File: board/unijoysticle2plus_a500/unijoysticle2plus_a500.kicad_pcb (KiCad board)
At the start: 4 copper layers, 62 x 49 mm, 44 parts, among them J1 DB9_Female, J2 DB9_Female, J3 USB_B_Micro, Q1 S8050, Q2 S8050, SW1 RESET, SW2 JOY SWAP, SW3 BOOT, U1 74HC05, U2 74HC05, U3 74HC05, U4 ESP32-WROOM-32E, U5 AMS1117-3.3, U6 CH340C

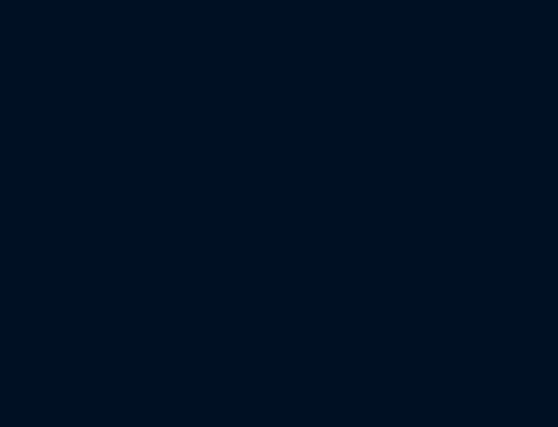
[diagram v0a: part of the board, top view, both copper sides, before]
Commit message: a500: remove duplicate symbols
It is able to run the EDR checks with 5 warnings.
Only one looks worth taking a look at.
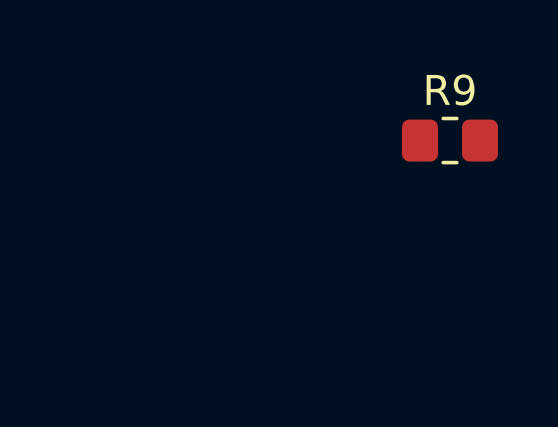
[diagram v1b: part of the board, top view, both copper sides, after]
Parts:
- added R9: 10k, Resistor_SMD:R_0805_2012Metric_Pad1.20x1.40mm_HandSolder, F.Cu at (151.9, 67.7)
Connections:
- net /ESP_BOOT renamed /ESP32/ESP_BOOT
- net /ESP_EN renamed /ESP32/ESP_EN
- net /ESP_RXD renamed UART_TX
- net /ESP_TXD renamed UART_RX
- net /GPIO34 renamed GPIO_SWITCH_USER1
- net /GPIO35 renamed GPIO_SWITCH_USER2
- net /GPIO39 renamed GPIO_39
- net /USBD+ renamed /USB Serial & Power/USBD+
- net /USBD- renamed /USB Serial & Power/USBD-
- C10 pad 2: GND -> GPIO_BOOTSTRAP_04
- C11 pad 2: GND -> GPIO_BOOTSTRAP_04
- C12 pad 1: GND -> GPIO_BOOTSTRAP_04
- C13 pad 1: GND -> GPIO_BOOTSTRAP_04
- C4 pad 2: GND -> GPIO_BOOTSTRAP_04
- C5 pad 2: GND -> GPIO_BOOTSTRAP_04
- C6 pad 1: GND -> GPIO_BOOTSTRAP_04
- C7 pad 2: GND -> GPIO_BOOTSTRAP_04
- C8 pad 2: GND -> GPIO_BOOTSTRAP_04
- C9 pad 2: GND -> GPIO_BOOTSTRAP_04
- H1 pad 1: GND -> GPIO_BOOTSTRAP_04
- H2 pad 1: GND -> GPIO_BOOTSTRAP_04
- J3 pad 5: GND -> GPIO_BOOTSTRAP_04
- Q1 pad 2: /RTS_PROG -> RTS_PROG
- Q2 pad 2: /DTR_PROG -> DTR_PROG
- R8 pad 1: Net-(Q2-Pad1) -> Net-(Q1-Pad1)
- R8 pad 2: /RTS_PROG -> DTR_PROG
- SW1 pad 1: GND -> GPIO_BOOTSTRAP_04
- SW3 pad 1: GND -> GPIO_BOOTSTRAP_04
- U4 pad 1: GND -> GPIO_BOOTSTRAP_04
- U4 pad 10: /GPIO_J2_DOWN -> GPIO_J2_DOWN
- U4 pad 11: /GPIO_J1_UP -> GPIO_J1_UP
- U4 pad 12: /GPIO_J2_UP -> GPIO_J2_UP
- U4 pad 13: /GPIO_J1_FIRE -> GPIO_J1_FIRE
- U4 pad 14: /GPIO_J2_LED -> GPIO_LED_J2
- U4 pad 15: GND -> GPIO_BOOTSTRAP_04
- U4 pad 16: /GPIO_J2_FIRE -> GPIO_J2_FIRE
- U4 pad 23: /GPIO_SWITCH_JOY -> GPIO_LED_BT
- U4 pad 26: GND -> GPIO_BOOTSTRAP_04
- U4 pad 27: /GPIO_J1_POTY -> GPIO_J1_POTY
- U4 pad 28: /GPIO_J2_RIGHT -> GPIO_J2_RIGHT
- U4 pad 29: /GPIO_J1_LED -> GPIO_LED_J1
- U4 pad 30: /GPIO_J1_DOWN -> GPIO_J1_DOWN
- U4 pad 31: /GPIO_J1_LEFT -> GPIO_J1_LEFT
- U4 pad 33: /GPIO_J2_POTX -> GPIO_J2_POTX
- U4 pad 36: /GPIO_J2_POTY -> GPIO_J2_POTY
- U4 pad 37: /GPIO_J1_RIGHT -> GPIO_J1_RIGHT
- U4 pad 38: GND -> GPIO_BOOTSTRAP_04
- U4 pad 39: GND -> GPIO_BOOTSTRAP_04
- U4 pad 4: /GPIO36 -> GPIO_BOOTSTRAP_04
- U4 pad 8: /GPIO_J2_LEFT -> GPIO_J2_LEFT
- U4 pad 9: /GPIO_J1_POTX -> GPIO_J1_POTX
- U5 pad 1: GND -> GPIO_BOOTSTRAP_04
- U6 pad 1: GND -> GPIO_BOOTSTRAP_04
- U6 pad 13: /DTR_PROG -> DTR_PROG
- U6 pad 14: /RTS_PROG -> RTS_PROG
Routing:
- net GPIO_BOOTSTRAP_04: track 0.00 -> 58.9 mm, vias 0 -> 30
- net GND: track 72.2 -> 13.3 mm, vias 41 -> 11
- net GPIO_J2_POTY: track 0.00 -> 52.0 mm, vias 0 -> 6
- net /GPIO_J2_POTY: track 52.0 -> 0.00 mm, vias 6 -> 0
- net GPIO_J1_UP: track 0.00 -> 50.0 mm, vias 0 -> 2
- net /GPIO_J1_UP: track 50.0 -> 0.00 mm, vias 2 -> 0
- net GPIO_J2_UP: track 0.00 -> 39.4 mm, vias 0 -> 2
- net /GPIO_J2_UP: track 39.4 -> 0.00 mm, vias 2 -> 0
- net GPIO_J1_FIRE: track 0.00 -> 38.4 mm, vias 0 -> 2
- net /GPIO_J1_FIRE: track 38.4 -> 0.00 mm, vias 2 -> 0
- net GPIO_J2_POTX: track 0.00 -> 38.3 mm, vias 0 -> 2
- net /GPIO_J2_POTX: track 38.3 -> 0.00 mm, vias 2 -> 0
- net GPIO_J2_LEFT: track 0.00 -> 37.6 mm, vias 0 -> 2
- net /GPIO_J2_LEFT: track 37.6 -> 0.00 mm, vias 2 -> 0
- net GPIO_J1_DOWN: track 0.00 -> 32.6 mm, vias 0 -> 2
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- added copper zone on In1.Cu, net GPIO_BOOTSTRAP_04
- added copper zone on In2.Cu, net GPIO_BOOTSTRAP_04
- removed copper zone on In1.Cu, net GND
- removed copper zone on In2.Cu, net GND

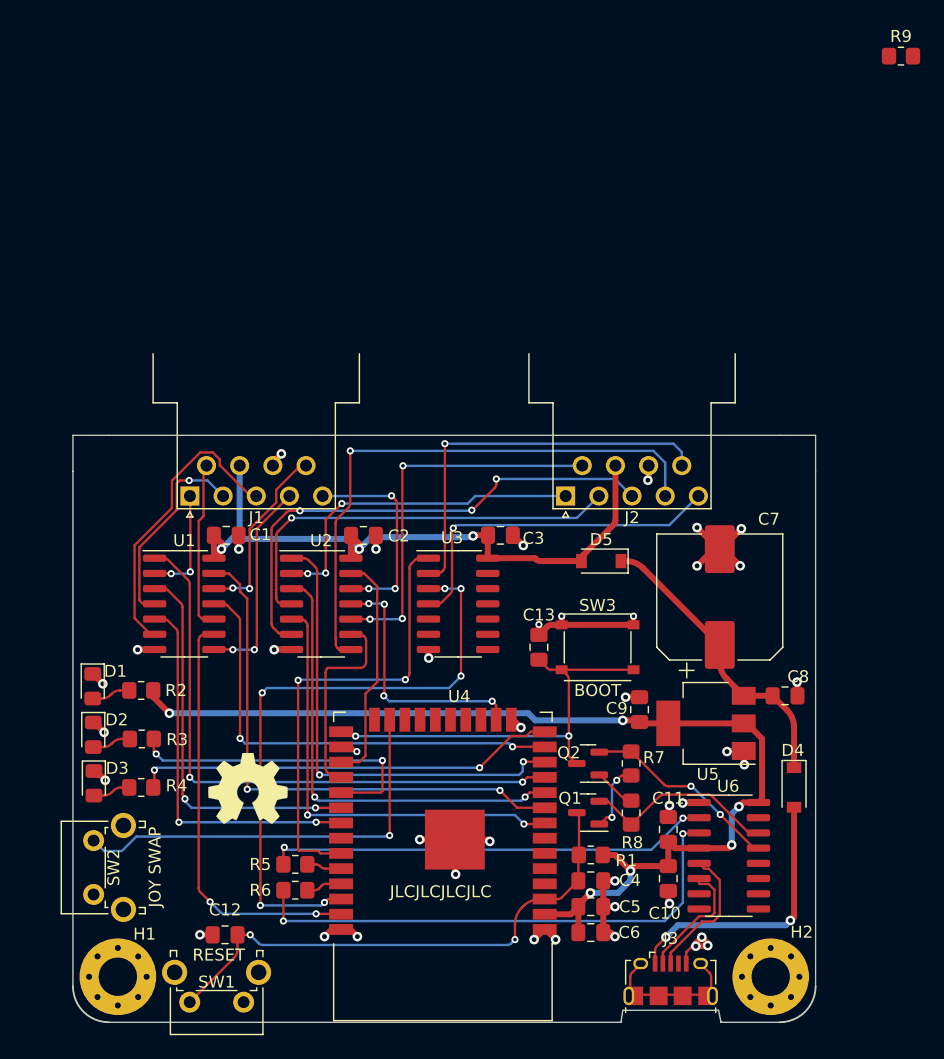
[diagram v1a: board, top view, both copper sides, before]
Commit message: uni2+ a500: schematic "ready"
The schematic should be "ready".
Layout WIP. Components were placed in "place".
But routing is missing, as well as logos
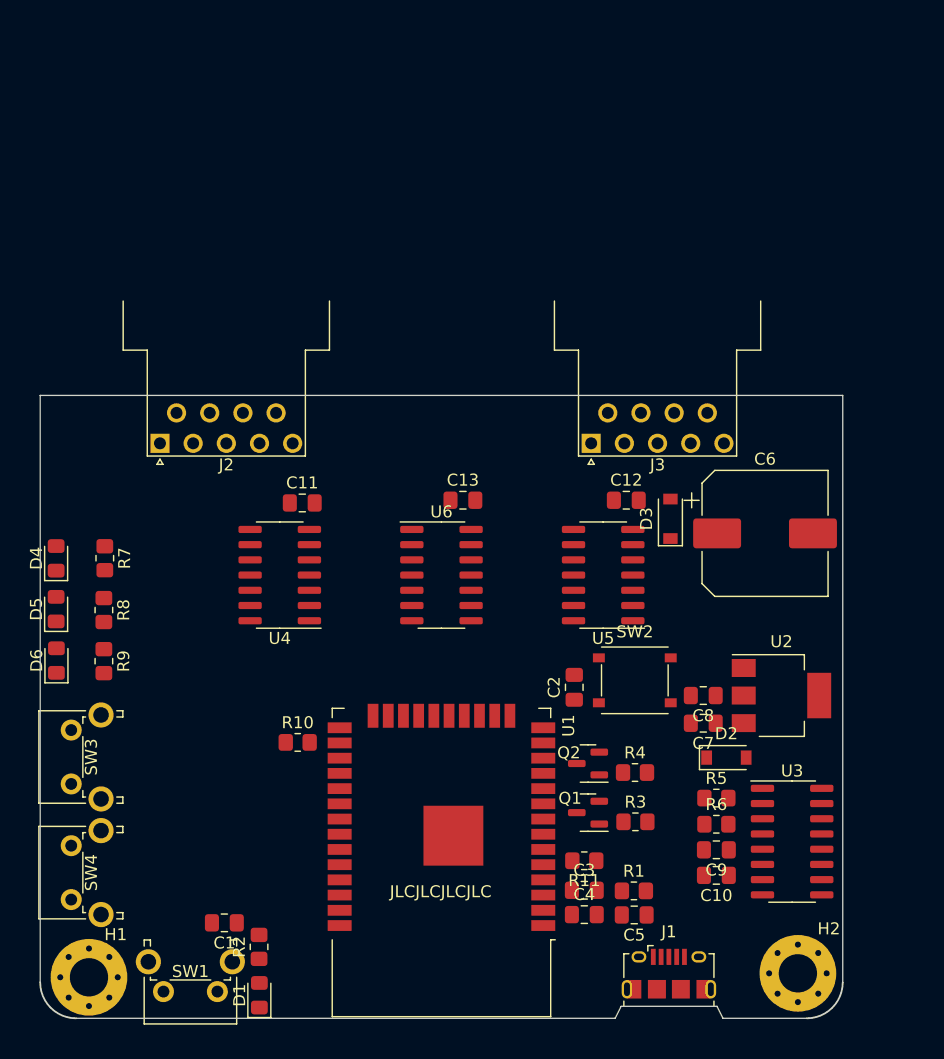
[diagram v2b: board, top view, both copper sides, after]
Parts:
- removed G***: LOGO, Unijoysticle:unijoysticle_logo_small
- removed REF**: OSHW-Symbol_6.7x6mm_SilkScreen, Symbol:OSHW-Symbol_6.7x6mm_SilkScreen
- added D6: RED, LED_SMD:LED_0805_2012Metric_Pad1.15x1.40mm_HandSolder, F.Cu at (81.4, 118.1)
- added R10: 0, Resistor_SMD:R_0805_2012Metric_Pad1.20x1.40mm_HandSolder, F.Cu at (101.5, 125.0)
- added R11: 0, Resistor_SMD:R_0805_2012Metric_Pad1.20x1.40mm_HandSolder, F.Cu at (125.4, 134.8)
- added SW4: USER2, Button_Switch_THT:SW_Tactile_SPST_Angled_PTS645Vx39-2LFS, F.Cu at (82.6, 138.1)
- C3: value .1uF -> 10uF
- C4: value 10uF -> .1uF
- C5: value .1uF -> 22uF
- C6: value 22uF -> 1000uF; footprint Capacitor_SMD:C_0805_2012Metric_Pad1.18x1.45mm_HandSolder -> Capacitor_SMD:CP_Elec_10x10
- C7: value 1000uF -> 22uF; footprint Capacitor_SMD:CP_Elec_10x10 -> Capacitor_SMD:C_0805_2012Metric_Pad1.18x1.45mm_HandSolder
- C9: value 22uF -> .1uF
- D1: value BLUE -> PWR
- D2: value GREEN -> 1N5819; footprint LED_SMD:LED_0805_2012Metric_Pad1.15x1.40mm_HandSolder -> Diode_SMD:D_SOD-123
- D3: value RED -> 1N5819; footprint LED_SMD:LED_0805_2012Metric_Pad1.15x1.40mm_HandSolder -> Diode_SMD:D_SOD-123
- D4: value 1N5819 -> BLUE; footprint Diode_SMD:D_SOD-123 -> LED_SMD:LED_0805_2012Metric_Pad1.15x1.40mm_HandSolder
- D5: value 1N5819 -> GREEN; footprint Diode_SMD:D_SOD-123 -> LED_SMD:LED_0805_2012Metric_Pad1.15x1.40mm_HandSolder
- J1: value DB9_Female -> USB_B_Micro; footprint Connector_Dsub:DSUB-9_Female_Horizontal_P2.77x2.54mm_EdgePinOffset9.40mm -> Connector_USB:USB_Micro-B_Amphenol_10118194_Horizontal
- J2: value DB9_Female -> PORT JOY #1
- J3: value USB_B_Micro -> PORT JOY #2; footprint Connector_USB:USB_Micro-B_Amphenol_10118194_Horizontal -> Connector_Dsub:DSUB-9_Female_Horizontal_P2.77x2.54mm_EdgePinOffset9.40mm
- R2: value 1.5k -> 1.5K
- R3, R4: value 1.5k -> 10k
- R7, R8, R9: value 10k -> 1.5K
- SW2: value JOY SWAP -> BOOT; footprint Button_Switch_THT:SW_Tactile_SPST_Angled_PTS645Vx39-2LFS -> Unijoysticle:SW_Push_1P1T_NO_5.1x5.1mm
- SW3: value BOOT -> USER1; footprint Unijoysticle:SW_Push_1P1T_NO_5.1x5.1mm -> Button_Switch_THT:SW_Tactile_SPST_Angled_PTS645Vx39-2LFS
- U1: value 74HC05 -> ESP32-WROOM-32E; footprint Package_SO:SOIC-14_3.9x8.7mm_P1.27mm -> RF_Module:ESP32-WROOM-32
- U2: value 74HC05 -> AMS1117-3.3; footprint Package_SO:SOIC-14_3.9x8.7mm_P1.27mm -> Package_TO_SOT_SMD:SOT-223-3_TabPin2
- U3: value 74HC05 -> CH340C; footprint Package_SO:SOIC-14_3.9x8.7mm_P1.27mm -> Package_SO:SOIC-16_3.9x9.9mm_P1.27mm
- U4: value ESP32-WROOM-32E -> 74HC05; footprint RF_Module:ESP32-WROOM-32 -> Package_SO:SOIC-14_3.9x8.7mm_P1.27mm
- U5: value AMS1117-3.3 -> 74HC05; footprint Package_TO_SOT_SMD:SOT-223-3_TabPin2 -> Package_SO:SOIC-14_3.9x8.7mm_P1.27mm
- U6: value CH340C -> 74HC05; footprint Package_SO:SOIC-16_3.9x9.9mm_P1.27mm -> Package_SO:SOIC-14_3.9x8.7mm_P1.27mm
- moved R9 83.5 mm to (85.3, 118.2), turned to -90 degrees
- moved D4 64.5 mm to (81.3, 109.6), turned to 90 degrees
- moved J1 56.5 mm to (132.5, 144.3), turned to 0 degrees
- moved D3 53.0 mm to (132.6, 106.3), turned to 90 degrees
- moved D2 52.9 mm to (137.3, 126.2), turned to 0 degrees
- moved C12 49.4 mm to (128.9, 104.7)
- moved SW2 48.6 mm to (129.6, 119.8), turned to 0 degrees
- moved R7 47.2 mm to (85.4, 109.6), turned to -90 degrees
- moved R8 47.2 mm to (85.3, 113.9)
- moved D5 45.7 mm to (81.3, 113.8), turned to 90 degrees
- moved SW3 45.4 mm to (82.6, 128.4), turned to 90 degrees
- moved J3 45.3 mm to (126.0, 100.0), turned to 180 degrees
- moved R3 41.8 mm to (129.7, 131.6)
- moved R4 41.2 mm to (129.7, 127.5)
- moved C11 40.9 mm to (101.9, 105.0), turned to 0 degrees
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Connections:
- C1 pad 1: +5V -> GND
- C1 pad 2: GND -> /ESP32/ESP_EN
- C10 pad 2: GPIO_BOOTSTRAP_04 -> GND
- C11 pad 1: +3V3 -> +5V
- C11 pad 2: GPIO_BOOTSTRAP_04 -> GND
- C12 pad 1: GPIO_BOOTSTRAP_04 -> +5V
- C12 pad 2: /ESP32/ESP_EN -> GND
- C13 pad 1: GPIO_BOOTSTRAP_04 -> +5V
- C13 pad 2: /ESP32/ESP_BOOT -> GND
- C2 pad 1: +5V -> GND
- C2 pad 2: GND -> /ESP32/ESP_BOOT
- C3 pad 1: +5V -> /ESP32/ESP_EN
- C4 pad 1: /ESP32/ESP_EN -> +3V3
- C4 pad 2: GPIO_BOOTSTRAP_04 -> GND
- C5 pad 1: +3V3 -> GND
- C5 pad 2: GPIO_BOOTSTRAP_04 -> +3V3
- C6 pad 1: GPIO_BOOTSTRAP_04 -> Net-(C6-Pad1)
- C6 pad 2: +3V3 -> GND
- C7 pad 1: Net-(C7-Pad1) -> Net-(C6-Pad1)
- C7 pad 2: GPIO_BOOTSTRAP_04 -> GND
- C8 pad 1: Net-(C7-Pad1) -> +3V3
- C8 pad 2: GPIO_BOOTSTRAP_04 -> GND
- C9 pad 2: GPIO_BOOTSTRAP_04 -> GND
- D2 pad 1: GND -> Net-(C6-Pad1)
- D2 pad 2: Net-(D2-Pad2) -> VBUS
- D3 pad 1: GND -> Net-(C6-Pad1)
- D3 pad 2: Net-(D3-Pad2) -> +5V
- D4 pad 1: Net-(C7-Pad1) -> GND
- D4 pad 2: VBUS -> Net-(D4-Pad2)
- D5 pad 1: Net-(C7-Pad1) -> GND
- D5 pad 2: +5V -> Net-(D5-Pad2)
- H1 pad 1: GPIO_BOOTSTRAP_04 -> GND
- H2 pad 1: GPIO_BOOTSTRAP_04 -> GND
- J1 pad 1: /J1_UP -> VBUS
- J1 pad 2: /J1_DOWN -> /USB Serial & Power/USBD-
- J1 pad 3: /J1_LEFT -> /USB Serial & Power/USBD+
- J1 pad 4: /J1_RIGHT -> unconnected-(J1-Pad4)
- J1 pad 5: /J1_POTY -> GND
- J1 pad 6: /J1_FIRE -> unconnected-(J1-Pad6)
- J2 pad 1: /J2_UP -> /Amiga Ports/J1_UP
- J2 pad 2: /J2_DOWN -> /Amiga Ports/J1_DOWN
- J2 pad 3: /J2_LEFT -> /Amiga Ports/J1_LEFT
- J2 pad 4: /J2_RIGHT -> /Amiga Ports/J1_RIGHT
- J2 pad 5: /J2_POTY -> /Amiga Ports/J1_POTY
- J2 pad 6: /J2_FIRE -> /Amiga Ports/J1_FIRE
- J2 pad 9: /J2_POTX -> /Amiga Ports/J1_POTX
- J3 pad 1: VBUS -> /Amiga Ports/J2_UP
- J3 pad 2: /USB Serial & Power/USBD- -> /Amiga Ports/J2_DOWN
- J3 pad 3: /USB Serial & Power/USBD+ -> /Amiga Ports/J2_LEFT
- J3 pad 4: unconnected-(J3-Pad4) -> /Amiga Ports/J2_RIGHT
- J3 pad 5: GPIO_BOOTSTRAP_04 -> /Amiga Ports/J2_POTY
- J3 pad 6: unconnected-(J3-Pad6) -> /Amiga Ports/J2_FIRE
- R3 pad 1: Net-(D2-Pad2) -> Net-(Q1-Pad1)
- R3 pad 2: /GPIO_J1_LED -> DTR_PROG
- R4 pad 1: Net-(D3-Pad2) -> Net-(Q2-Pad1)
- R4 pad 2: /GPIO_J2_LED -> RTS_PROG
- R7 pad 1: Net-(Q1-Pad1) -> Net-(D4-Pad2)
- R7 pad 2: /DTR_PROG -> GPIO_LED_BT
- R8 pad 1: Net-(Q1-Pad1) -> Net-(D5-Pad2)
- R8 pad 2: DTR_PROG -> GPIO_LED_J1
- R9 pad 1: Net-(Q2-Pad1) -> Net-(D6-Pad2)
- R9 pad 2: RTS_PROG -> GPIO_LED_J2
- SW1 pad 1: GPIO_BOOTSTRAP_04 -> GND
- SW2 pad 2: /GPIO_SWITCH_JOY -> /ESP32/ESP_BOOT
- SW3 pad 1: GPIO_BOOTSTRAP_04 -> GND
- SW3 pad 2: /ESP32/ESP_BOOT -> GPIO_SWITCH_USER1
- U1 pad 1: /GPIO_J1_UP -> GND
- U1 pad 10: /J1_FIRE -> GPIO_J2_DOWN
- U1 pad 11: /GPIO_J1_FIRE -> GPIO_J1_UP
- U1 pad 12: /J1_POTX -> GPIO_J2_UP
- U1 pad 13: /GPIO_J1_POTX -> GPIO_J1_FIRE
- U1 pad 14: +5V -> GPIO_LED_J2
- U1 pad 2: /J1_UP -> +3V3
- U1 pad 3: /GPIO_J1_DOWN -> /ESP32/ESP_EN
- U1 pad 4: /J1_DOWN -> GPIO_BOOTSTRAP_36
- U1 pad 5: /GPIO_J1_LEFT -> GPIO_39
- U1 pad 6: /J1_LEFT -> GPIO_SWITCH_USER1
- U1 pad 7: GND -> GPIO_SWITCH_USER2
- U1 pad 8: /J1_RIGHT -> GPIO_J2_LEFT
- U1 pad 9: /GPIO_J1_RIGHT -> GPIO_J1_POTX
- U2 pad 1: /GPIO_J2_UP -> GND
- U2 pad 2: /J2_UP -> +3V3
- U2 pad 3: /GPIO_J2_DOWN -> Net-(C6-Pad1)
- U3 pad 1: /GPIO_J2_POTX -> GND
- U3 pad 10: (no net) -> unconnected-(U3-Pad10)
- U3 pad 11: (no net) -> unconnected-(U3-Pad11)
- U3 pad 12: (no net) -> unconnected-(U3-Pad12)
- U3 pad 13: (no net) -> DTR_PROG
- U3 pad 14: +5V -> RTS_PROG
- U3 pad 2: /J2_POTX -> Net-(R5-Pad2)
- U3 pad 3: /GPIO_J2_POTY -> Net-(R6-Pad2)
- U3 pad 4: /J2_POTY -> +3V3
- U3 pad 5: (no net) -> /USB Serial & Power/USBD+
- U3 pad 6: (no net) -> /USB Serial & Power/USBD-
- U3 pad 7: GND -> unconnected-(U3-Pad7)
- U3 pad 8: (no net) -> unconnected-(U3-Pad8)
- U3 pad 9: (no net) -> unconnected-(U3-Pad9)
- U4 pad 1: GPIO_BOOTSTRAP_04 -> GPIO_J1_UP
- U4 pad 10: GPIO_J2_DOWN -> /Amiga Ports/J1_FIRE
- U4 pad 11: GPIO_J1_UP -> GPIO_J1_FIRE
- U4 pad 12: GPIO_J2_UP -> (no net)
- U4 pad 13: GPIO_J1_FIRE -> (no net)
- U4 pad 14: GPIO_LED_J2 -> +5V
- U4 pad 2: +3V3 -> /Amiga Ports/J1_UP
- U4 pad 3: /ESP32/ESP_EN -> GPIO_J1_DOWN
- U4 pad 4: GPIO_BOOTSTRAP_04 -> /Amiga Ports/J1_DOWN
- U4 pad 5: GPIO_39 -> GPIO_J1_LEFT
- U4 pad 6: GPIO_SWITCH_USER1 -> /Amiga Ports/J1_LEFT
- U4 pad 7: GPIO_SWITCH_USER2 -> GND
- U4 pad 8: GPIO_J2_LEFT -> /Amiga Ports/J1_RIGHT
- U4 pad 9: GPIO_J1_POTX -> GPIO_J1_RIGHT
- U5 pad 1: GPIO_BOOTSTRAP_04 -> GPIO_J2_UP
- U5 pad 2: +3V3 -> /Amiga Ports/J2_UP
- U5 pad 3: Net-(C7-Pad1) -> GPIO_J2_DOWN
- U6 pad 1: GPIO_BOOTSTRAP_04 -> GPIO_J1_POTX
- U6 pad 10: unconnected-(U6-Pad10) -> /Amiga Ports/J2_POTY
- U6 pad 11: unconnected-(U6-Pad11) -> GPIO_J2_POTY
- U6 pad 12: unconnected-(U6-Pad12) -> /Amiga Ports/J2_POTX
- U6 pad 13: DTR_PROG -> GPIO_J2_POTX
- U6 pad 14: RTS_PROG -> +5V
- U6 pad 2: Net-(R5-Pad2) -> /Amiga Ports/J1_POTX
- U6 pad 3: Net-(R6-Pad2) -> GPIO_J1_POTY
- U6 pad 4: +3V3 -> /Amiga Ports/J1_POTY
- U6 pad 5: /USB Serial & Power/USBD+ -> (no net)
- U6 pad 6: /USB Serial & Power/USBD- -> (no net)
- U6 pad 7: unconnected-(U6-Pad7) -> GND
- U6 pad 8: unconnected-(U6-Pad8) -> (no net)
- U6 pad 9: unconnected-(U6-Pad9) -> (no net)
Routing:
- net +3V3: track 88.7 -> 0.00 mm, vias 6 -> 0
- net GPIO_BOOTSTRAP_04: track 58.9 -> 0.00 mm, vias 30 -> 0
- net +5V: track 57.5 -> 0.00 mm, vias 3 -> 0
- net GPIO_J2_POTY: track 52.0 -> 0.00 mm, vias 6 -> 0
- net GPIO_J1_UP: track 50.0 -> 0.00 mm, vias 2 -> 0
- net /J2_RIGHT: track 47.6 -> 0.00 mm, vias 1 -> 0
- net /GPIO_J1_POTX: track 45.4 -> 0.00 mm, vias 2 -> 0
- net /ESP32/ESP_EN: track 45.0 -> 0.00 mm, vias 2 -> 0
- net Net-(R6-Pad2): track 43.7 -> 0.00 mm, vias 2 -> 0
- net /J2_LEFT: track 42.8 -> 0.00 mm, vias 3 -> 0
- net GPIO_J2_UP: track 39.4 -> 0.00 mm, vias 2 -> 0
- net GPIO_J1_FIRE: track 38.4 -> 0.00 mm, vias 2 -> 0
- net /GPIO_J2_DOWN: track 38.3 -> 0.00 mm, vias 2 -> 0
- net GPIO_J2_POTX: track 38.3 -> 0.00 mm, vias 2 -> 0
- net GPIO_J2_LEFT: track 37.6 -> 0.00 mm, vias 2 -> 0
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- removed copper zone on In1.Cu, net GPIO_BOOTSTRAP_04
- removed copper zone on In2.Cu, net GPIO_BOOTSTRAP_04
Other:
- board size 62 x 49 mm -> 67 x 52 mm
- board text added: "Unijoysticle 2+ A500 Rev. A"
- board text removed: "Unijoysticle 2+ Rev. H"

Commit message: uni a500: manual routing
WIP... all wires connected. requires to double check everything
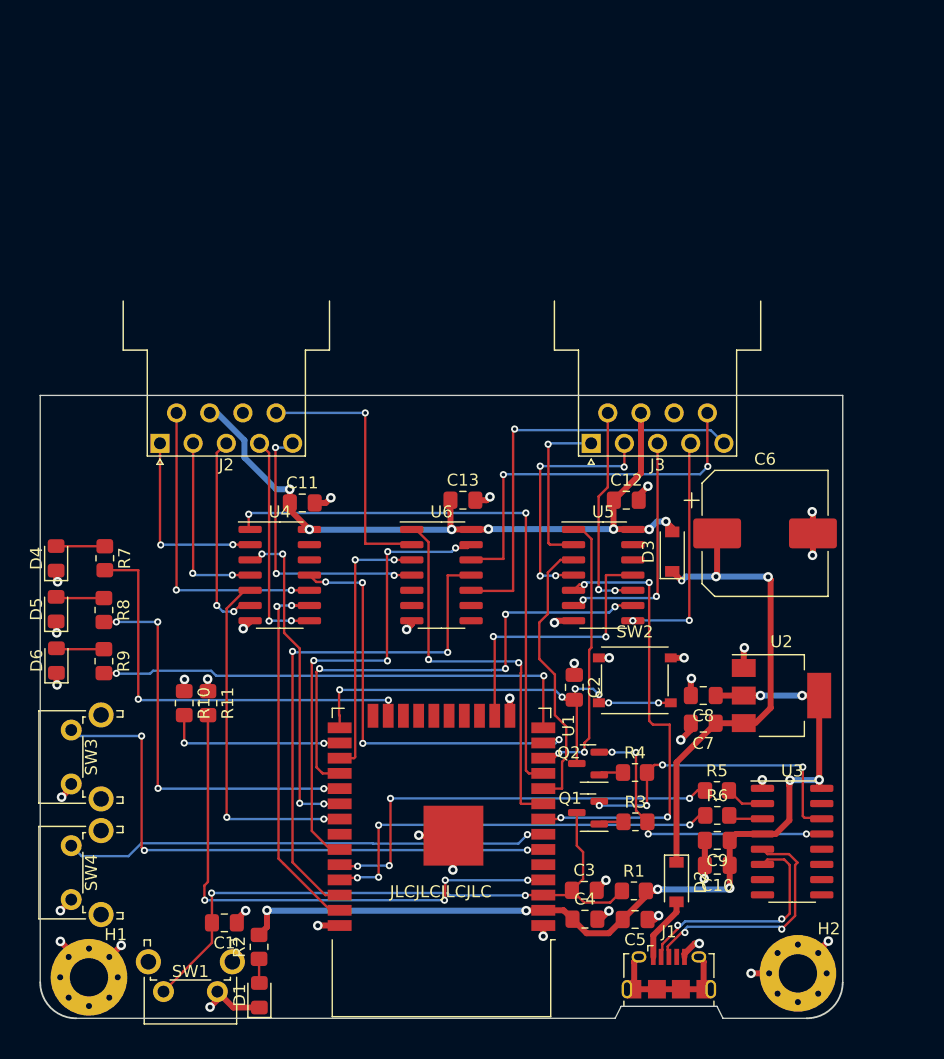
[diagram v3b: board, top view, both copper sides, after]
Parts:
- moved R11 34.1 mm to (94.0, 121.7), turned to -90 degrees
- moved D2 11.2 mm to (133.1, 136.6), turned to -90 degrees
- moved R10 10.0 mm to (92.0, 121.7), turned to -90 degrees
- moved D3 2.75 mm to (132.8, 109.0)
- moved C10 0.84 mm to (136.5, 135.2)
- moved C9 0.79 mm to (136.5, 133.1)
- moved R6 0.74 mm to (136.5, 131.1)
- moved R5 0.64 mm to (136.5, 129.0)
- moved C5 0.39 mm to (129.7, 139.8)
- moved C4 0.38 mm to (125.5, 139.7)
- turned C2 to -90 degrees
- turned U4 to 0 degrees
- turned U5 to 0 degrees
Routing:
- net +3V3: track 0.00 -> 75.6 mm, vias 0 -> 8
- net GND: track 0.00 -> 66.8 mm, vias 0 -> 38
- net +5V: track 0.00 -> 58.8 mm, vias 0 -> 7
- net /ESP32/ESP_EN: track 0.00 -> 52.4 mm, vias 0 -> 2
- net GPIO_SWITCH_USER1: track 0.00 -> 49.2 mm, vias 0 -> 3
- net GPIO_J1_UP: track 0.00 -> 47.5 mm, vias 0 -> 2
- net GPIO_BOOTSTRAP_36: track 0.00 -> 45.5 mm, vias 0 -> 4
- net GPIO_J2_POTY: track 0.00 -> 44.2 mm, vias 0 -> 2
- net GPIO_J2_RIGHT: track 0.00 -> 41.6 mm, vias 0 -> 4
- net GPIO_LED_J2: track 0.00 -> 41.5 mm, vias 0 -> 2
- net GPIO_SWITCH_USER2: track 0.00 -> 40.6 mm, vias 0 -> 1
- net Net-(C6-Pad1): track 0.00 -> 40.3 mm, vias 0 -> 3
- net GPIO_J2_POTX: track 0.00 -> 39.8 mm, vias 0 -> 4
- net /ESP32/ESP_BOOT: track 0.00 -> 38.4 mm, vias 0 -> 6
- net GPIO_J2_LEFT: track 0.00 -> 38.2 mm, vias 0 -> 4
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- added copper zone on In1.Cu, net GND
- added copper zone on In2.Cu, net GND

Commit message: a500: fix most of the warnings in the PCB
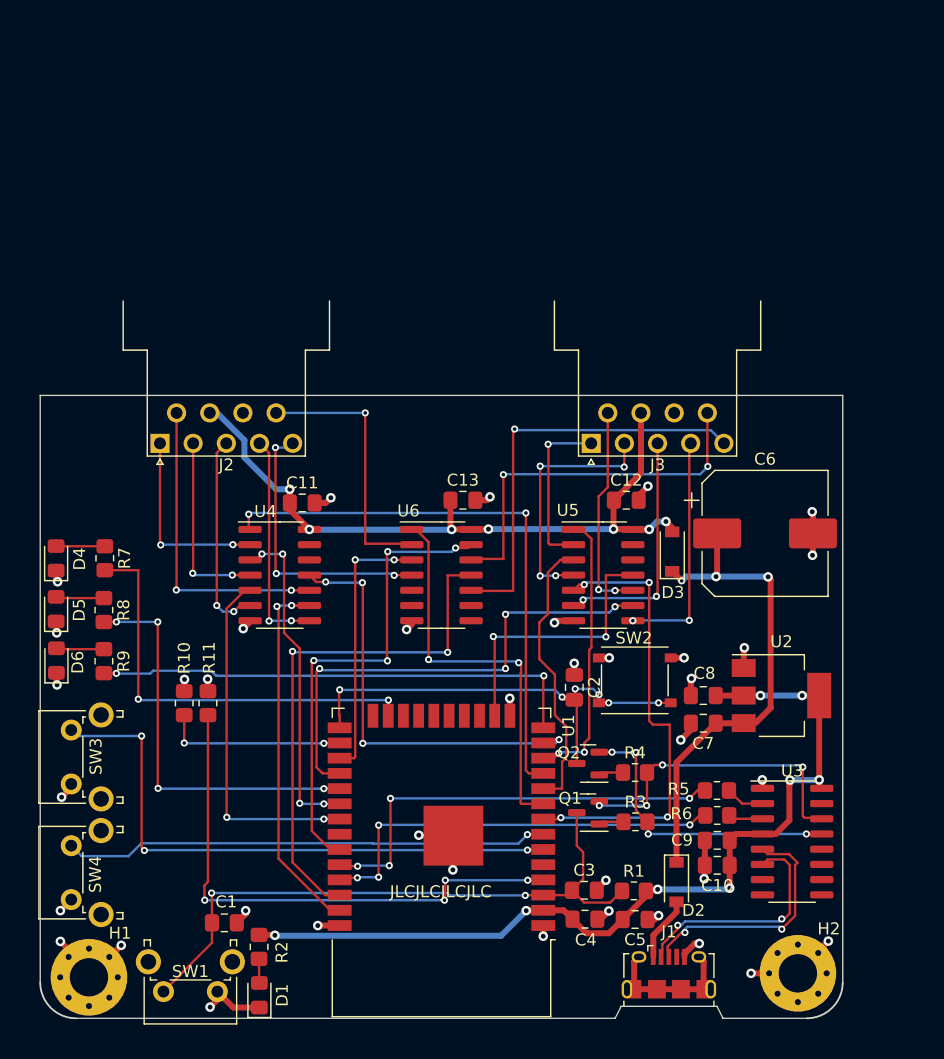
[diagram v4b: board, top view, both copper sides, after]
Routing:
- net +3V3: track 75.6 -> 74.8 mm
